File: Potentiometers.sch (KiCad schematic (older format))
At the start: 20 parts, among them J10 AccelConn, J11 BrakeConn, J12 AccelConn2, J13 BrakeConn2

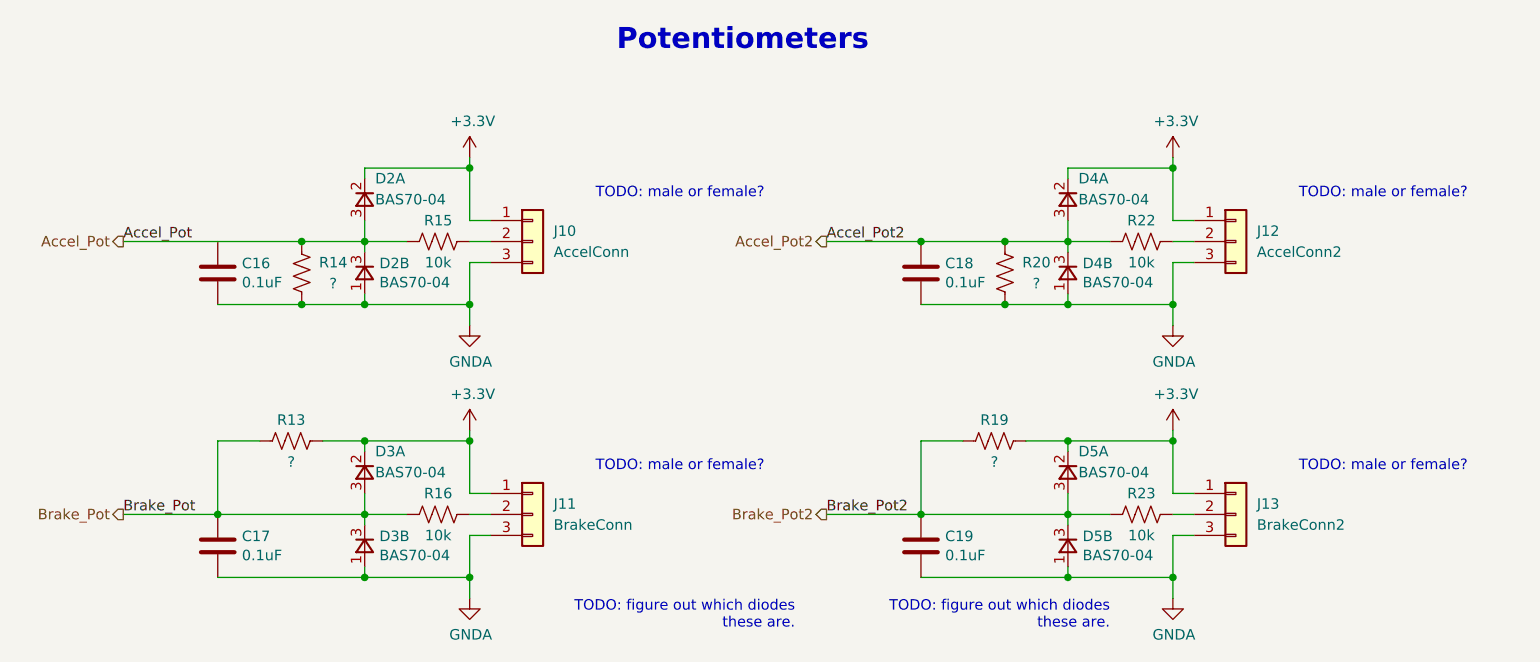
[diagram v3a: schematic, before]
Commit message: Makes the 12V and GNDPWR traces bigger
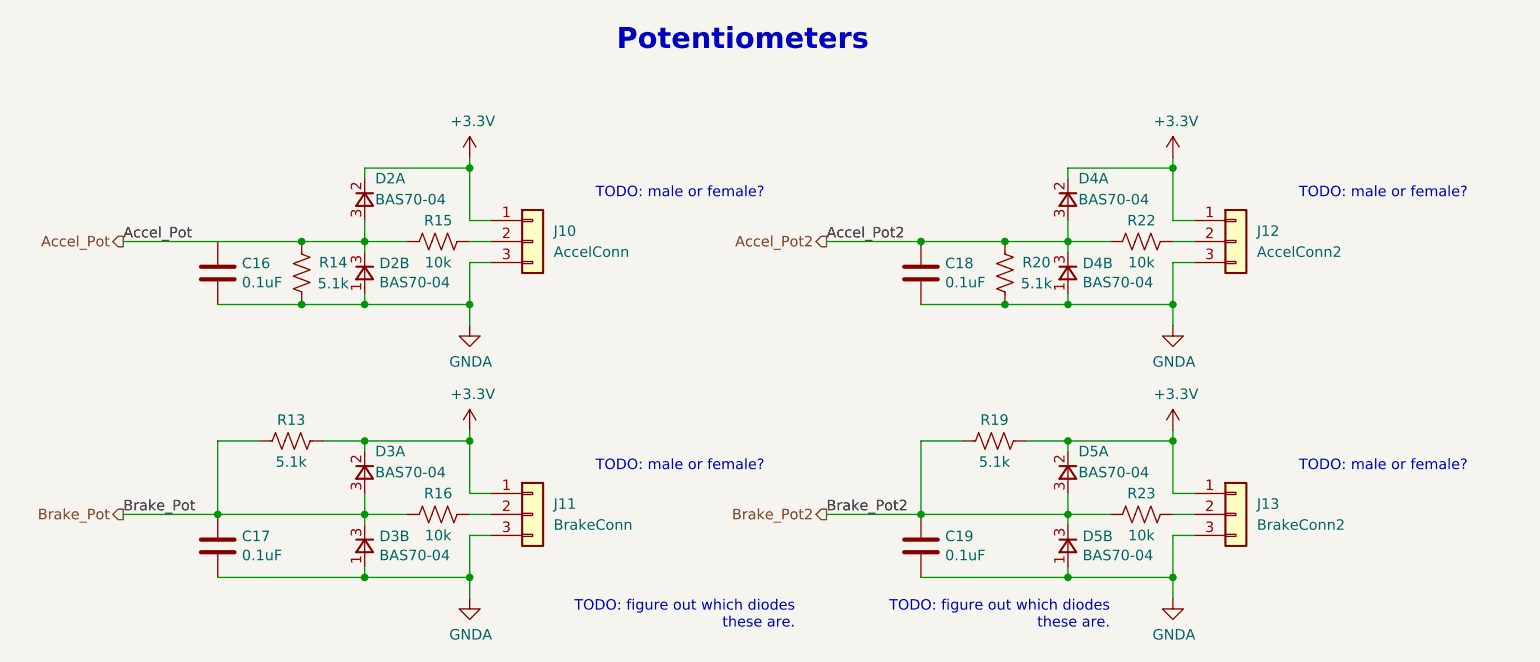
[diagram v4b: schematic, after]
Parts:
- R13, R14, R19, R20: value ? -> 5.1k
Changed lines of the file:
@@
 AR Path="/5FA99DC3/5FAAA5EC" Ref="R13"  Part="1"
 F 0 "R13" V 3550 4100 50  0000 C CNN
-F 1 "?" V 3750 4100 50  0000 C CNN
+F 1 "5.1k" V 3750 4100 50  0000 C CNN
 F 2 "Resistor_SMD:R_0805_2012Metric" V 3690 4090 50  0001 C CNN
 F 3 "~" H 3650 4100 50  0001 C CNN
@@
 AR Path="/5FA99DC3/5FAAA5F3" Ref="R19"  Part="1"
 F 0 "R19" V 6900 4100 50  0000 C CNN
-F 1 "?" V 7100 4100 50  0000 C CNN
+F 1 "5.1k" V 7100 4100 50  0000 C CNN
 F 2 "Resistor_SMD:R_0805_2012Metric" V 7040 4090 50  0001 C CNN
 F 3 "~" H 7000 4100 50  0001 C CNN
@@
 AR Path="/5FA99DC3/5FAAA5FA" Ref="R14"  Part="1"
 F 0 "R14" H 3850 3350 50  0000 C CNN
-F 1 "?" H 3850 3250 50  0000 C CNN
+F 1 "5.1k" H 3850 3250 50  0000 C CNN
 F 2 "Resistor_SMD:R_0805_2012Metric" V 3740 3290 50  0001 C CNN
 F 3 "~" H 3700 3300 50  0001 C CNN
@@
 AR Path="/5FA99DC3/5FAAA605" Ref="R20"  Part="1"
 F 0 "R20" H 7200 3350 50  0000 C CNN
-F 1 "?" H 7200 3250 50  0000 C CNN
+F 1 "5.1k" H 7200 3250 50  0000 C CNN
 F 2 "Resistor_SMD:R_0805_2012Metric" V 7090 3290 50  0001 C CNN
 F 3 "~" H 7050 3300 50  0001 C CNN

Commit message: removes the isp
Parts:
- D2, D3, D4, D5: symbol utsvt-chips:BAS70-04 -> Dashboard-rescue:BAS70-04-utsvt-chips
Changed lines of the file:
@@
 TODO: figure out which diodes\nthese are.
 $Comp
-L utsvt-chips:BAS70-04 D?
+L Dashboard-rescue:BAS70-04-utsvt-chips D?
 U 1 1 5FAAA588
 P 7350 2950
@@
 	7350 3450 7850 3450
 $Comp
-L utsvt-chips:BAS70-04 D?
+L Dashboard-rescue:BAS70-04-utsvt-chips D?
 U 1 1 5FAAA59D
 P 7350 4250
@@
 	3300 3450 3700 3450
 $Comp
-L utsvt-chips:BAS70-04 D?
+L Dashboard-rescue:BAS70-04-utsvt-chips D?
 U 1 1 5FAAA5B3
 P 4000 2950
@@
 	3300 4750 4000 4750
 $Comp
-L utsvt-chips:BAS70-04 D?
+L Dashboard-rescue:BAS70-04-utsvt-chips D?
 U 1 1 5FAAA5C5
 P 4000 4250
@@
 Brake_Pot2
 $Comp
-L utsvt-chips:BAS70-04 D2
+L Dashboard-rescue:BAS70-04-utsvt-chips D2
 U 2 1 5F7BB467
 P 4000 3300
@@
 $EndComp
 $Comp
-L utsvt-chips:BAS70-04 D3
+L Dashboard-rescue:BAS70-04-utsvt-chips D3
 U 2 1 5F7BC260
 P 4000 4600
@@
 $EndComp
 $Comp
-L utsvt-chips:BAS70-04 D4
+L Dashboard-rescue:BAS70-04-utsvt-chips D4
 U 2 1 5F7BC9B9
 P 7350 3300
@@
 $EndComp
 $Comp
-L utsvt-chips:BAS70-04 D5
+L Dashboard-rescue:BAS70-04-utsvt-chips D5
 U 2 1 5F7BD2F1
 P 7350 4600
